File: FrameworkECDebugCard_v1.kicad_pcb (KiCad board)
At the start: 2 copper layers, 26 x 30 mm, 18 parts, among them P1 USB_C_Plug_USB2.0, P2 USB_B_Micro, U1 FT230XS

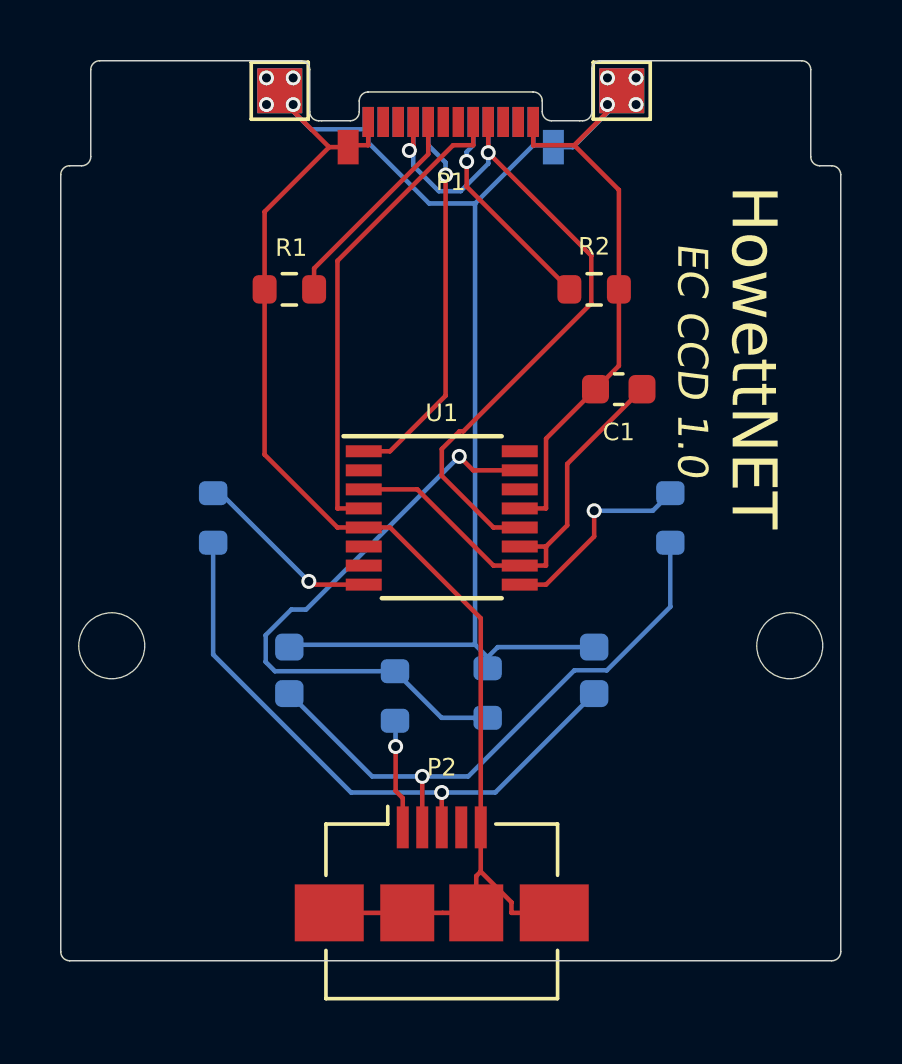
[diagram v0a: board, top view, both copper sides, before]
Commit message: v1.1: switch to FT230XQ (QFN) and 0402 components instead of 0603
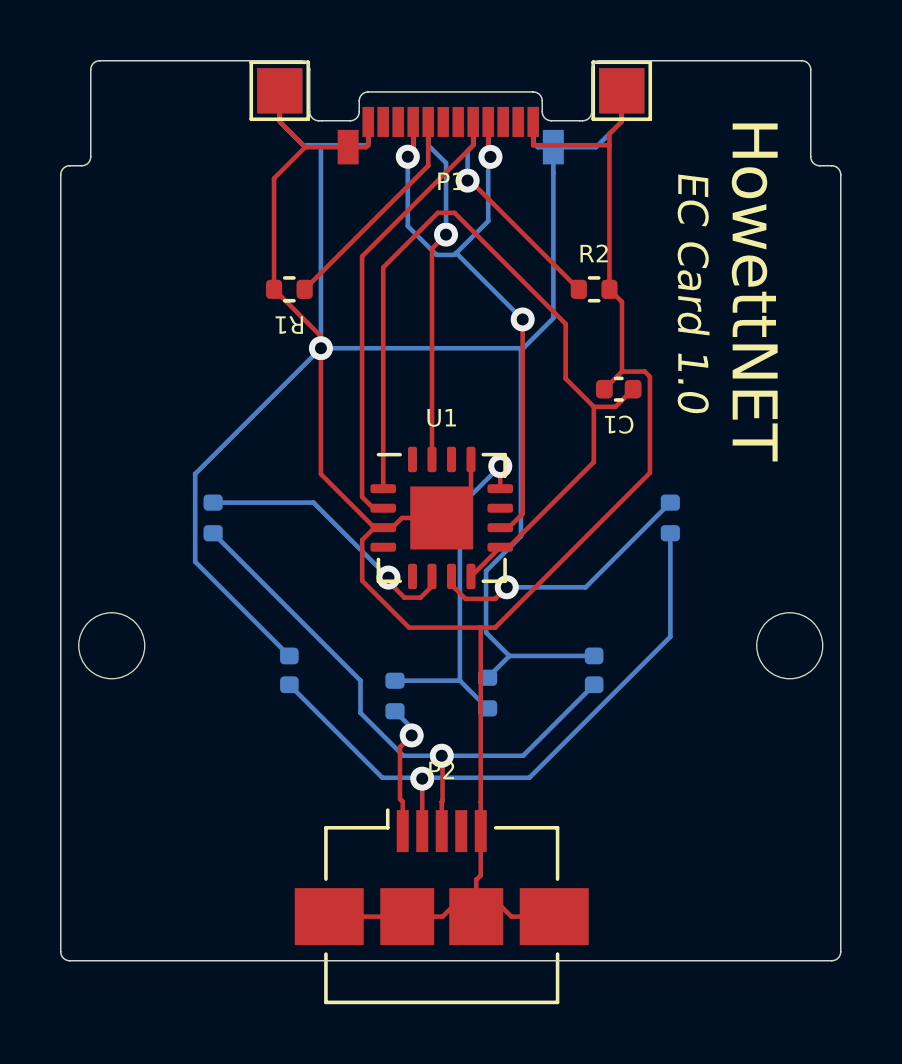
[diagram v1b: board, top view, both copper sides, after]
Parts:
- C1, C2, C3: footprint Capacitor_SMD:C_0603_1608Metric -> Capacitor_SMD:C_0402_1005Metric
- R1, R2, R3, R4, R5, R6: footprint Resistor_SMD:R_0603_1608Metric -> Resistor_SMD:R_0402_1005Metric
- U1: value FT230XS -> FT230XQ; footprint Package_SO:SSOP-16_3.9x4.9mm_P0.635mm -> Package_DFN_QFN:QFN-16-1EP_4x4mm_P0.65mm_EP2.1x2.1mm
- moved P2 0.12 mm to (139.7, 154.2)
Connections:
- P1 pad A8: Net-(U1-Pad4) -> Net-(P1-PadA8)
- U1 pad 1: Net-(P1-PadB8) -> Net-(C1-Pad1)
- U1 pad 10: Net-(C1-Pad1) -> VBUS
- U1 pad 11: Net-(C1-Pad1) -> unconnected-(U1-Pad11)
- U1 pad 12: VBUS -> Net-(R3-Pad1)
- U1 pad 15: Net-(R3-Pad1) -> Net-(P1-PadB8)
- U1 pad 2: unconnected-(U1-Pad2) -> Net-(P1-PadA8)
- U1 pad 3: Net-(C1-Pad1) -> GND
- U1 pad 4: Net-(U1-Pad4) -> unconnected-(U1-Pad4)
- U1 pad 5: GND -> unconnected-(U1-Pad5)
- U1 pad 6: unconnected-(U1-Pad6) -> Net-(R5-Pad2)
- U1 pad 7: unconnected-(U1-Pad7) -> Net-(R6-Pad2)
- U1 pad 8: Net-(R5-Pad2) -> Net-(C1-Pad1)
- U1 pad 9: Net-(R6-Pad2) -> Net-(C1-Pad1)
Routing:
- net GND: track 108.0 -> 133.3 mm, vias 8 -> 1
- net Net-(U1-Pad4): track 16.0 -> 0.00 mm
- net Net-(P1-PadA8): track 0.00 -> 14.9 mm
- net Net-(C1-Pad1): track 15.2 -> 28.0 mm
- net Net-(R3-Pad1): track 20.2 -> 11.9 mm
- net Net-(R5-Pad2): track 6.28 -> 9.17 mm
- net VBUS: track 25.9 -> 23.5 mm, vias 2 -> 3
- net Net-(R6-Pad2): track 6.79 -> 9.10 mm
- net Net-(P1-PadB8): track 12.9 -> 11.7 mm
- net Net-(C3-Pad1): track 20.0 -> 21.2 mm
- net Net-(C2-Pad1): track 20.9 -> 19.9 mm
- net VCC: track 3.66 -> 4.42 mm
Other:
- board text added: "EC Card 1.0"
- board text removed: "EC CCD 1.0"

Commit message: Schematic: clarify VBUS_{HOST,DEV}, reorganize to avoid flyover wires
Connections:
- net VBUS renamed VBUS_DEV
- net VCC renamed VBUS_HOST

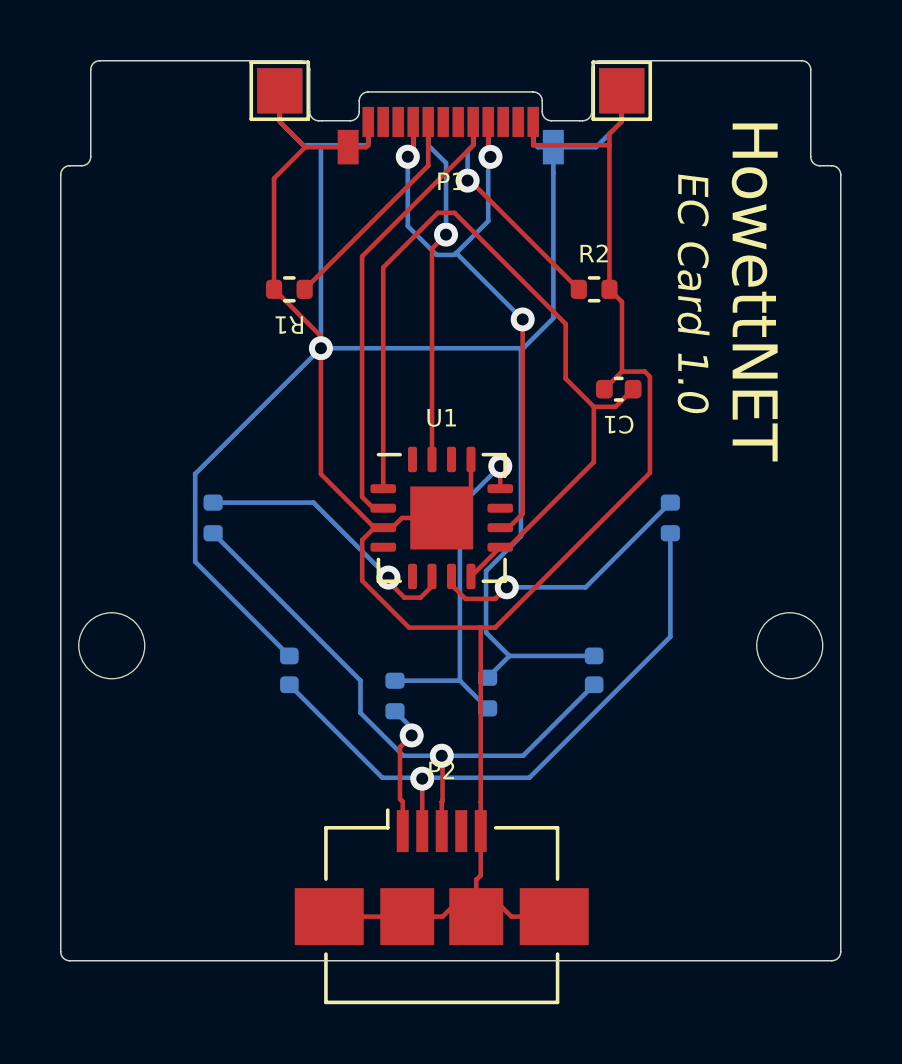
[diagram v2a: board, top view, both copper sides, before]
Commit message: Rework board per Kieran's suggestions
- Route the USB differential pairs together, and without vias
	- Had to move back to the SSOP package because the QFN package
	  would require a crossover (yes, no, it doesn't make any sense)
- Ground fill
- Hand-route
- Redistribute passives to be more reasonably laid out
- Power the FTDI chip off VBUS_HOST instead of VBUS_DEV
- Add TX/RX LEDs
- Add a ferrite bead
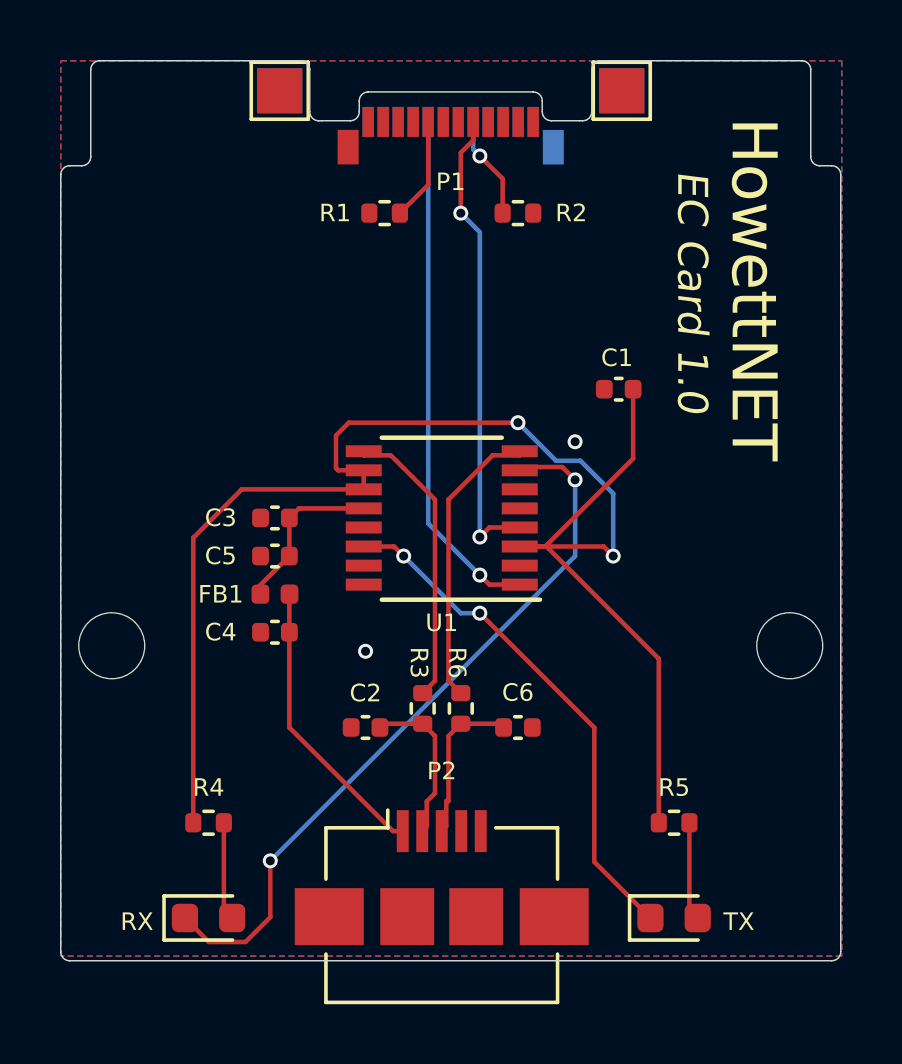
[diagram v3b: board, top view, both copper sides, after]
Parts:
- removed the R3 at (138.1, 148.2)
- added C3: 100nf, Capacitor_SMD:C_0402_1005Metric, F.Cu at (134.1, 142.2)
- added C4: 10nf, Capacitor_SMD:C_0402_1005Metric, F.Cu at (134.1, 146.1)
- added C5: 4.7uF, Capacitor_SMD:C_0402_1005Metric, F.Cu at (134.1, 143.5)
- added D1: Green, LED_SMD:LED_0603_1608Metric, F.Cu at (131.9, 155.6)
- added D2: Red, LED_SMD:LED_0603_1608Metric, F.Cu at (147.4, 155.6)
- added FB1: 500mA, Inductor_SMD:L_0402_1005Metric, F.Cu at (134.1, 144.8)
- added R5: 270R, Resistor_SMD:R_0402_1005Metric, F.Cu at (147.4, 152.4)
- C2: renamed from C3; moved to F.Cu
- C6: renamed from C2; moved to F.Cu
- R3: renamed from R6; moved to F.Cu
- R4: value 10k -> 270R; moved to F.Cu
- R6: renamed from R5; moved to F.Cu
- U1: value FT230XQ -> FT230XS; footprint Package_DFN_QFN:QFN-16-1EP_4x4mm_P0.65mm_EP2.1x2.1mm -> Package_SO:SSOP-16_3.9x4.9mm_P0.635mm
- moved R3 10.4 mm to (139.1, 148.6)
- moved R6 10.4 mm to (140.3, 148.6)
- moved R4 10.3 mm to (131.9, 152.4), turned to 0 degrees
- moved R1 4.07 mm to (137.8, 132.1)
- moved R2 3.59 mm to (142.2, 132.1)
- moved C2 3.17 mm to (137.2, 149.2), turned to 180 degrees
- moved C6 3.17 mm to (142.2, 149.2), turned to 0 degrees
- turned U1 to 180 degrees
- renumbered TP4 to TP3, TP3 to TP4
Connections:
- net Net-(C2-Pad1) renamed /USBD+
- net Net-(C3-Pad1) renamed /USBD-
- C1 pad 1: Net-(C1-Pad1) -> VCCIO
- P1 pad A8: Net-(U1-Pad2) -> /DOUT
- P1 pad B8: Net-(U1-Pad15) -> /DIN
- P2 pad 1: VBUS_HOST -> Net-(C4-Pad1)
- R3 pad 2: Net-(R6-Pad2) -> /F_USBD-
- R4 pad 1: GND -> VCCIO
- R4 pad 2: Net-(U1-Pad12) -> Net-(D1-Pad2)
- R6 pad 2: Net-(R5-Pad2) -> /F_USBD+
- U1 pad 1: Net-(C1-Pad1) -> /DIN
- U1 pad 10: VBUS_DEV -> VCCIO
- U1 pad 11: unconnected-(U1-Pad11) -> VCCIO
- U1 pad 12: Net-(U1-Pad12) -> VBUS_HOST
- U1 pad 14: unconnected-(U1-Pad14) -> /TXLED
- U1 pad 15: Net-(U1-Pad15) -> unconnected-(U1-Pad15)
- U1 pad 2: Net-(U1-Pad2) -> unconnected-(U1-Pad2)
- U1 pad 3: GND -> VCCIO
- U1 pad 4: unconnected-(U1-Pad4) -> /DOUT
- U1 pad 5: unconnected-(U1-Pad5) -> GND
- U1 pad 6: Net-(R5-Pad2) -> unconnected-(U1-Pad6)
- U1 pad 7: Net-(R6-Pad2) -> /RXLED
- U1 pad 8: Net-(C1-Pad1) -> /F_USBD+
- U1 pad 9: Net-(C1-Pad1) -> /F_USBD-
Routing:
- net GND: track 133.3 -> 0.00 mm, vias 1 -> 2
- net VCCIO: track 0.00 -> 53.2 mm, vias 0 -> 2
- net Net-(C1-Pad1): track 28.0 -> 0.00 mm
- net /RXLED: track 0.00 -> 23.8 mm, vias 0 -> 2
- net VBUS_DEV: track 23.5 -> 0.00 mm, vias 3 -> 0
- net /TXLED: track 0.00 -> 17.3 mm, vias 0 -> 2
- net /DIN: track 0.00 -> 17.3 mm, vias 0 -> 1
- net /USBD-: track 21.2 -> 5.40 mm, vias 1 -> 0
- net /DOUT: track 0.00 -> 15.7 mm, vias 0 -> 2
- net Net-(U1-Pad2): track 14.9 -> 0.00 mm
- net /USBD+: track 19.9 -> 5.36 mm, vias 1 -> 0
- net Net-(U1-Pad12): track 11.9 -> 0.00 mm, vias 1 -> 0
- net Net-(U1-Pad15): track 11.7 -> 0.00 mm, vias 1 -> 0
- net /F_USBD-: track 0.00 -> 9.74 mm
- net /F_USBD+: track 0.00 -> 9.74 mm
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- added copper zone on B.Cu, net GND
- added copper zone on F.Cu, net GND
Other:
- board text added: "RX"
- board text added: "TX"

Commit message: Add a 1x5 header to break out the EC/FTDI pins
This header uses the SparkFun "LOCK" footprint, which should
allow me to click in a header without soldering it down.
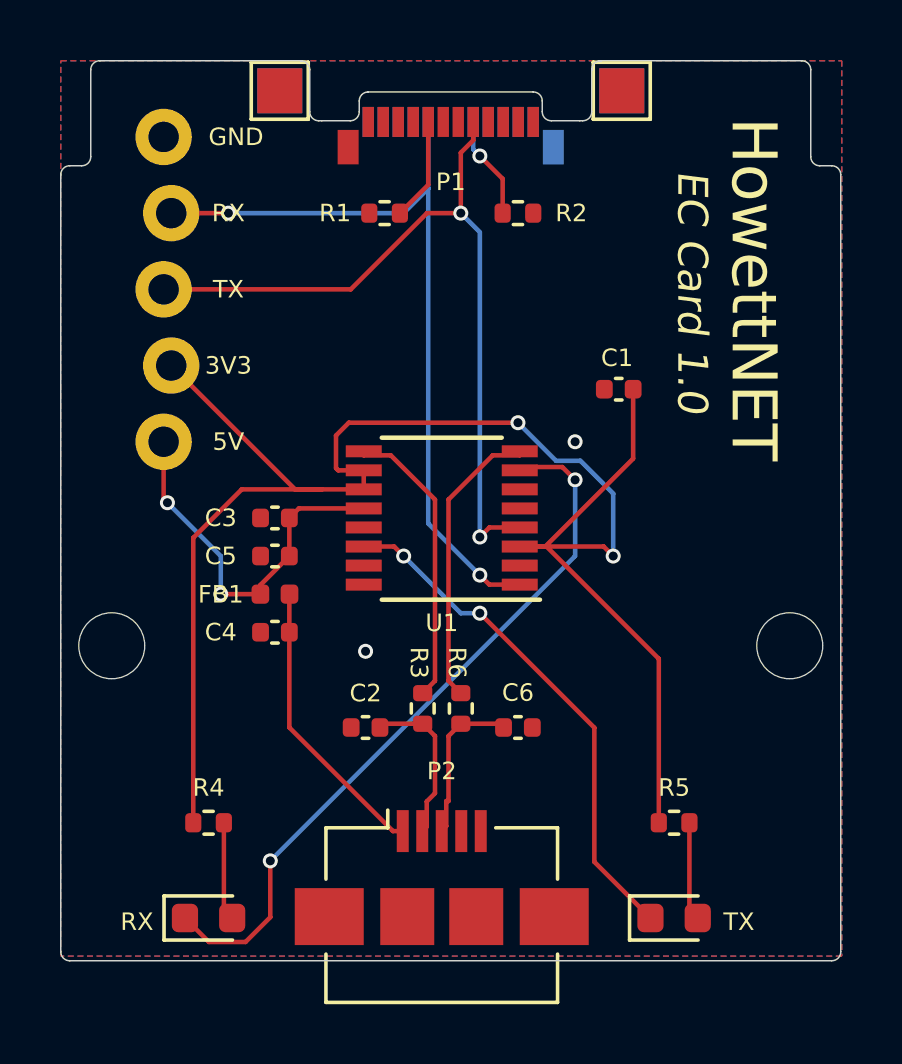
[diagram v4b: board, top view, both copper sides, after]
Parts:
- added J1: Conn_01x05, FrameworkECDebugCard_v1:1X05_LOCK, F.Cu at (130.6, 139.7)
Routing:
- net /DOUT: track 15.7 -> 26.7 mm
- net /DIN: track 17.3 -> 26.2 mm, vias 1 -> 2
- net VBUS_HOST: track 5.55 -> 12.7 mm, vias 0 -> 2
- net VCCIO: track 53.2 -> 59.9 mm
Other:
- board text added: "3V3"
- board text added: "5V"
- board text added: "GND"
- board text added: "TX/RX header is from EC perspective TX comes {dblquote}out{dblquote} of EC; RX goes {dblquote}in{dblquote}"

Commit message: Re-route the USB differential pairs following the DigiKey guide
These traces are *C H O N K Y*
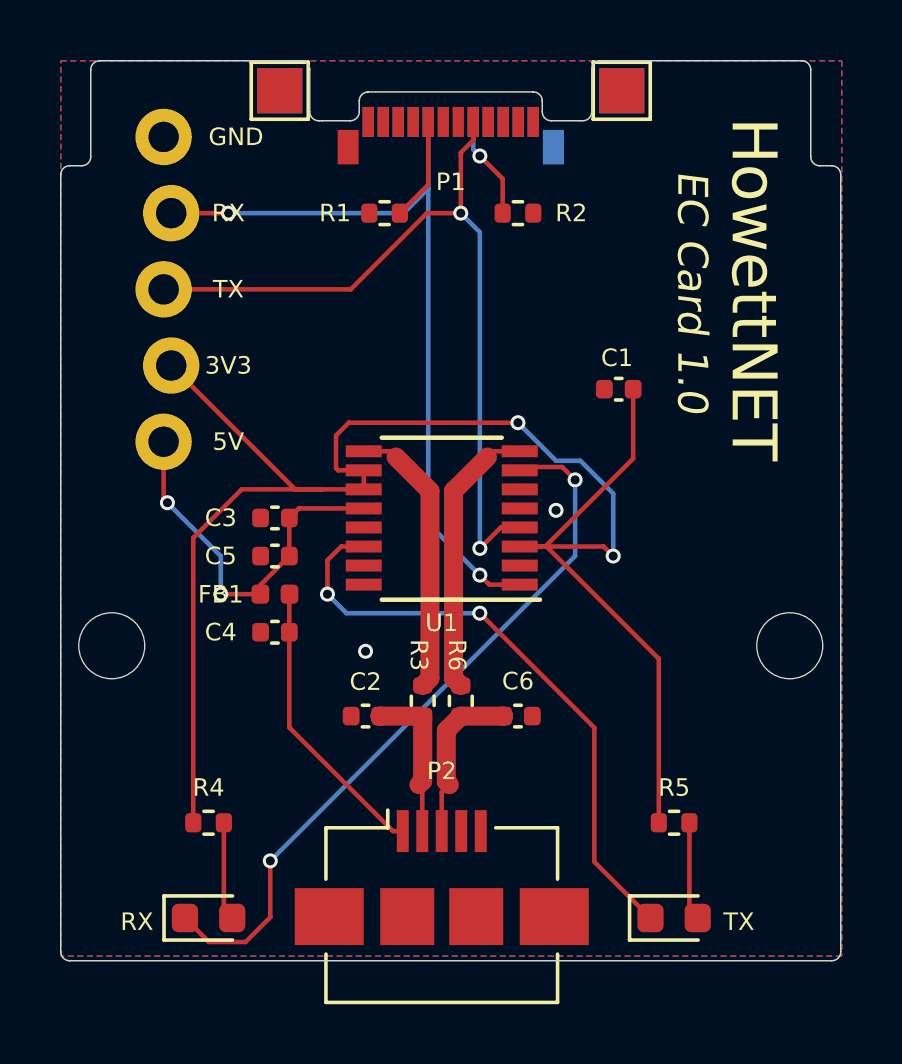
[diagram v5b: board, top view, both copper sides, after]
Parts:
- moved C2 0.38 mm to (137.2, 148.8)
- moved C6 0.38 mm to (142.2, 148.8)
- moved R3 0.25 mm to (139.1, 148.3)
- moved R6 0.25 mm to (140.3, 148.3)
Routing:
- net /TXLED: track 17.3 -> 20.4 mm
- net /DOUT: track 26.7 -> 27.2 mm

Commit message: Delete the unused pads from USB C to pass DRC?
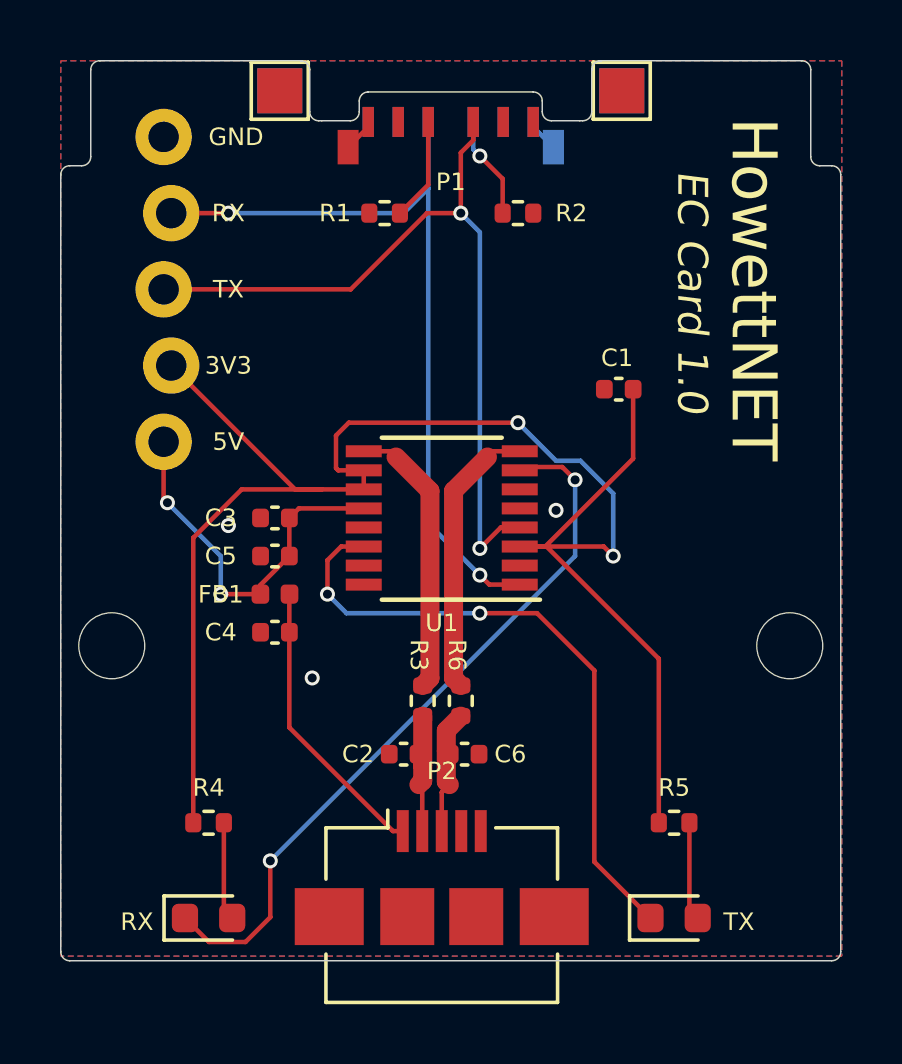
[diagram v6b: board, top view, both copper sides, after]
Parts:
- moved C6 2.18 mm to (140.5, 150.1)
- moved C2 1.80 mm to (138.4, 150.1)
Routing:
- net GND: track 0.00 -> 2.24 mm, vias 2 -> 3
- net /USBD+: track 5.61 -> 4.18 mm
- net /USBD-: track 5.36 -> 4.15 mm
- net /TXLED: track 20.4 -> 21.5 mm
